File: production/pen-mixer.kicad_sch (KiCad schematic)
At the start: 31 parts, among them J1 USB-C 16P, J2 BAT, J3 FSR, U1 ISP1807-LR, U2 LSM6DS3TR-C, U3 MCP73831T-2ACI/OT, U4 TPS7A0533PDBV

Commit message: radio symbol 60mm t-split normalize
Claude-Session: https://claude.ai/code/session_01RCYT2QSY7BVZDeTyE9KrC4
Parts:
- U1: BOM Comments (none) -> 0 stock at JLC/LCSC - source from Mouser or DigiKey; LCSC (none) -> C5264268; MPN (none) -> ISP1807-LR-RS; Manufacturer (none) -> Insight SiP

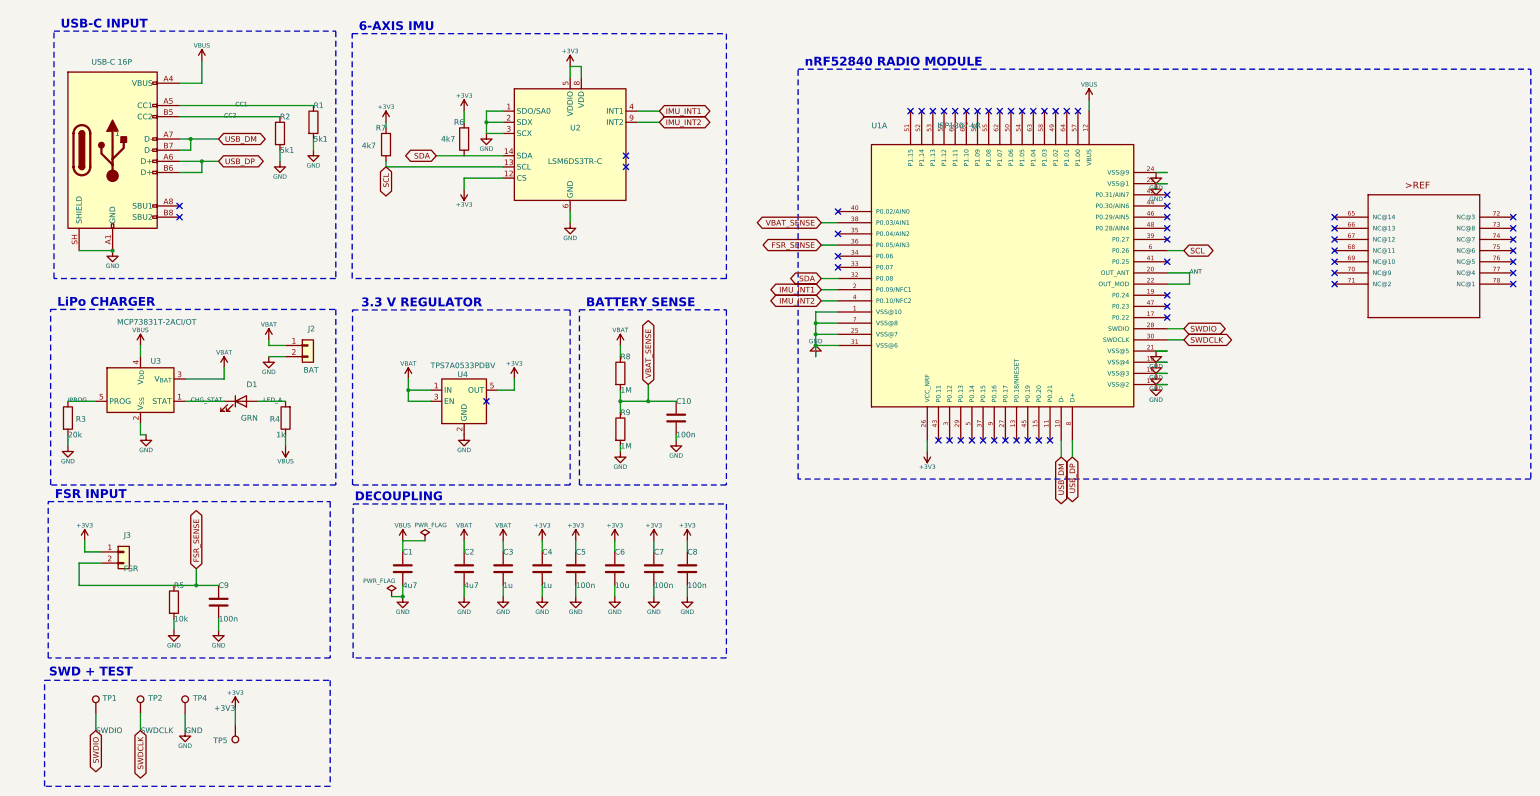
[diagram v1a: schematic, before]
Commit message: label based connectivity for fragile nets
Claude-Session: https://claude.ai/code/session_01RCYT2QSY7BVZDeTyE9KrC4
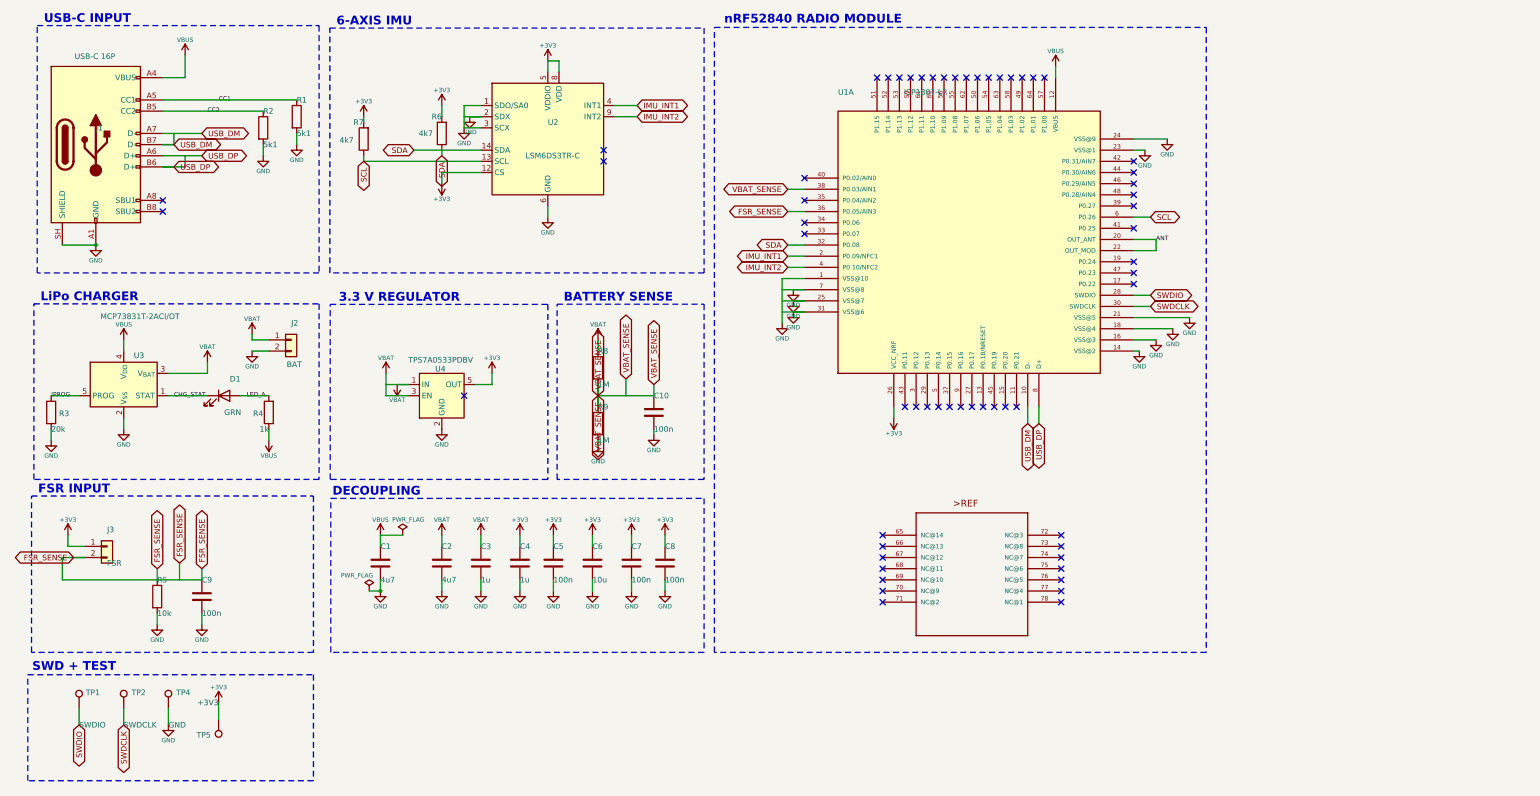
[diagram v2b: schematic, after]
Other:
- title: Pen Mixer v0.1 - pen-mounted motion controller -> Pen Mixer v0.1
- moved on the sheet: C1, C10, C2, C3, C4, C5, C6, C7, C8, C9, D1, J1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

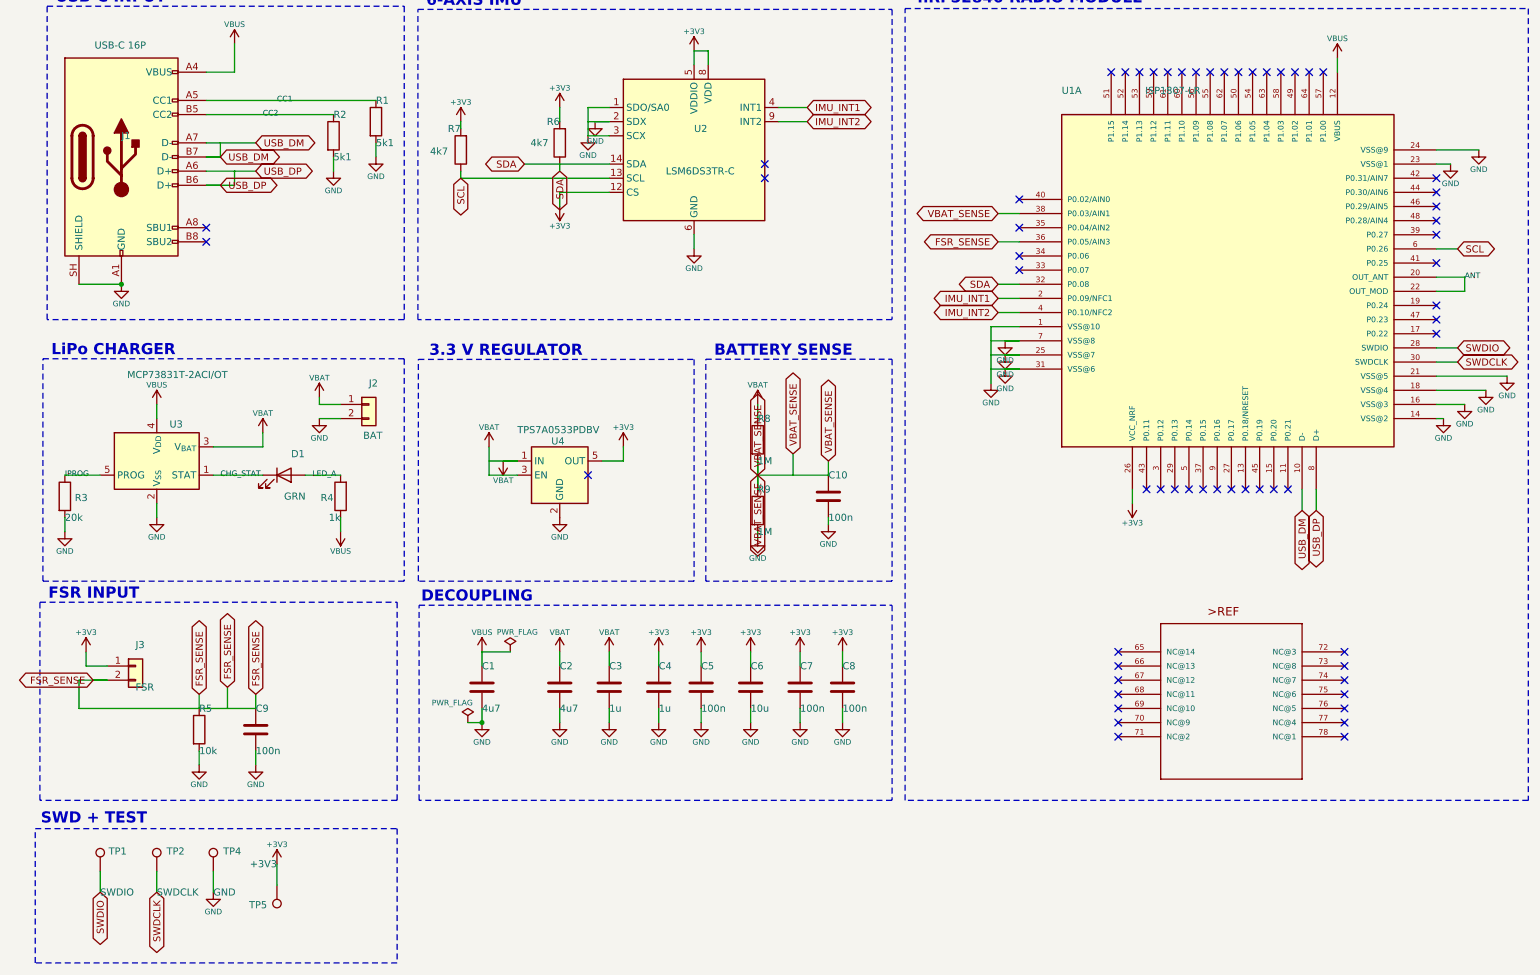
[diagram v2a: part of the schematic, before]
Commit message: remove fsr rearrange back pads
Claude-Session: https://claude.ai/code/session_01RCYT2QSY7BVZDeTyE9KrC4
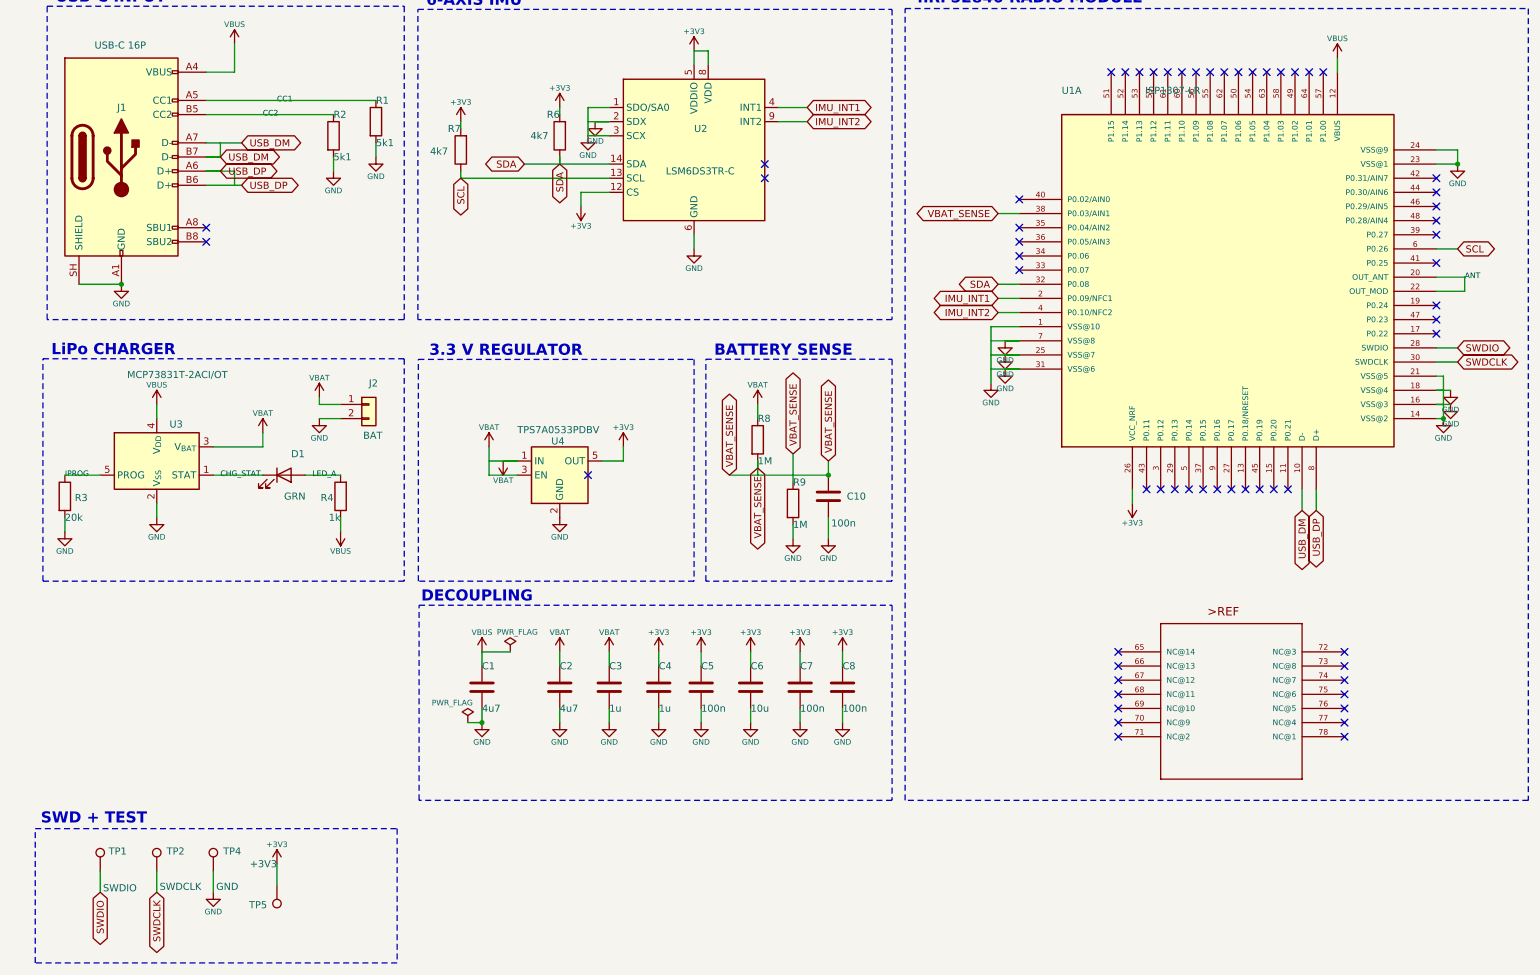
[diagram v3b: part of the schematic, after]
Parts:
- removed C9: 100n, Capacitor_SMD:C_0402_1005Metric, symbol Device:C
- removed J3: FSR, pen-mixer:SolderPad_1.2x2.0mm, symbol Connector_Generic:Conn_01x02
- removed R5: 10k, Resistor_SMD:R_0402_1005Metric, symbol Device:R
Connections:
- net FSR_SENSE: no longer names the net of U1.36 (P0.05/AIN3)
- no-connect marks 59 -> 60
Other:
- note removed: "FSR INPUT"
- moved on the sheet: R6, R9

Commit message: pads to board extremes
Claude-Session: https://claude.ai/code/session_01RCYT2QSY7BVZDeTyE9KrC4
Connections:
- net GND: no longer U1.25 (VSS@7), U1.31 (VSS@6), U1.7 (VSS@8), U2.2 (SDX)
- net VBAT: no longer U4.1 (IN)

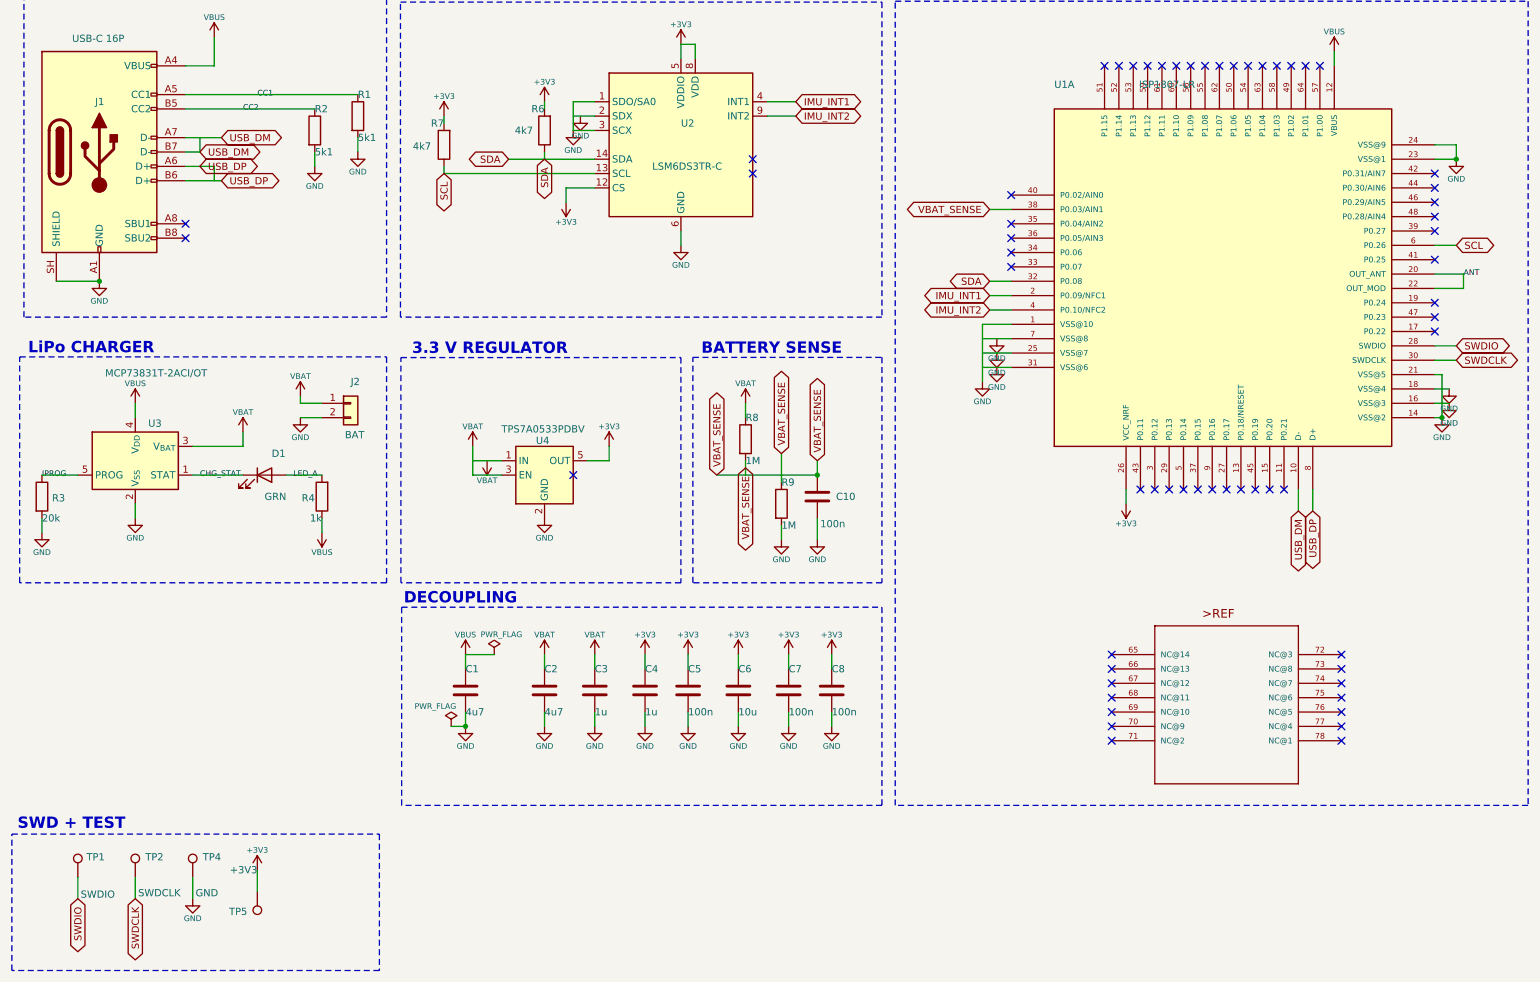
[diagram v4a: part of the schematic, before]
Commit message: fix wire tee gaps
Claude-Session: https://claude.ai/code/session_01RCYT2QSY7BVZDeTyE9KrC4
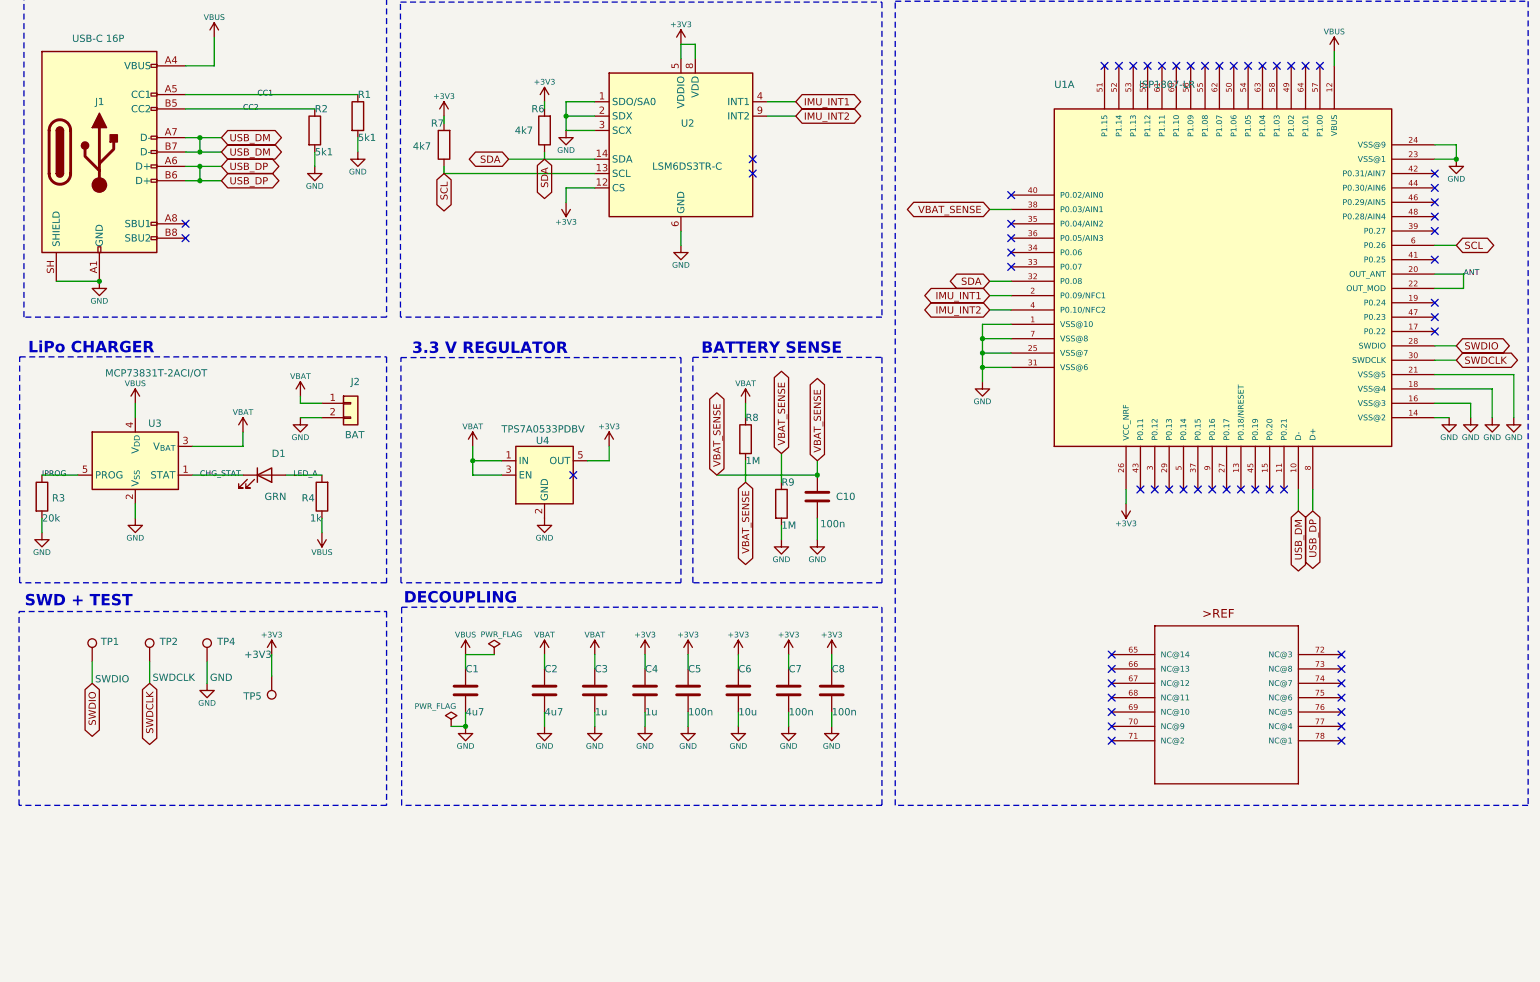
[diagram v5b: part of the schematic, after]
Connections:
- net GND: now also U1.25 (VSS@7), U1.31 (VSS@6), U1.7 (VSS@8), U2.2 (SDX)
- net VBAT: now also U4.1 (IN)
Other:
- moved on the sheet: TP1, TP2, TP4, TP5

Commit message: redhat styled boms
Claude-Session: https://claude.ai/code/session_01RCYT2QSY7BVZDeTyE9KrC4
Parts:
- C1, C2: LCSC (none) -> C23733; MPN (none) -> CL05A475MP5NRNC; Manufacturer (none) -> Samsung Electro-Mechanics
- C10, C5, C7, C8: LCSC (none) -> C1525; MPN (none) -> CL05B104KO5NNNC; Manufacturer (none) -> Samsung Electro-Mechanics
- C3, C4: LCSC (none) -> C52923; MPN (none) -> CL05A105KA5NQNC; Manufacturer (none) -> Samsung Electro-Mechanics
- C6: LCSC (none) -> C23692971; MPN (none) -> CGA0402X5R106M6R3GT; Manufacturer (none) -> TDK
- D1: LCSC (none) -> C130723; MPN (none) -> NCD0402G1; Manufacturer (none) -> Foshan NationStar
- J1: LCSC (none) -> C2988369; MPN (none) -> GT-USB-7010ASV; Manufacturer (none) -> G-Switch
- R1, R2: LCSC (none) -> C25905; MPN (none) -> 0402WGF5101TCE; Manufacturer (none) -> UNI-ROYAL
- R3: LCSC (none) -> C25765; MPN (none) -> 0402WGF2002TCE; Manufacturer (none) -> UNI-ROYAL
- R4: LCSC (none) -> C11702; MPN (none) -> 0402WGF1001TCE; Manufacturer (none) -> UNI-ROYAL
- R6, R7: LCSC (none) -> C25900; MPN (none) -> 0402WGF4701TCE; Manufacturer (none) -> UNI-ROYAL
- R8, R9: LCSC (none) -> C26083; MPN (none) -> 0402WGF1004TCE; Manufacturer (none) -> UNI-ROYAL
- U2: LCSC (none) -> C967633; MPN (none) -> LSM6DS3TR-C; Manufacturer (none) -> STMicroelectronics
- U3: LCSC (none) -> C424093; MPN (none) -> MCP73831T-2ACI/OT; Manufacturer (none) -> Microchip
- U4: LCSC (none) -> C493453; MPN (none) -> TPS7A0533PDBVR; Manufacturer (none) -> Texas Instruments
